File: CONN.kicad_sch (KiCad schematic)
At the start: 11 parts, among them J1 Conn_01x15, J2 Conn_01x15, J4 Conn_ARM_SWD_TagConnect_TC203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, J5 USB_C_Plug_USB2.0, U6 USBLC6-2P6

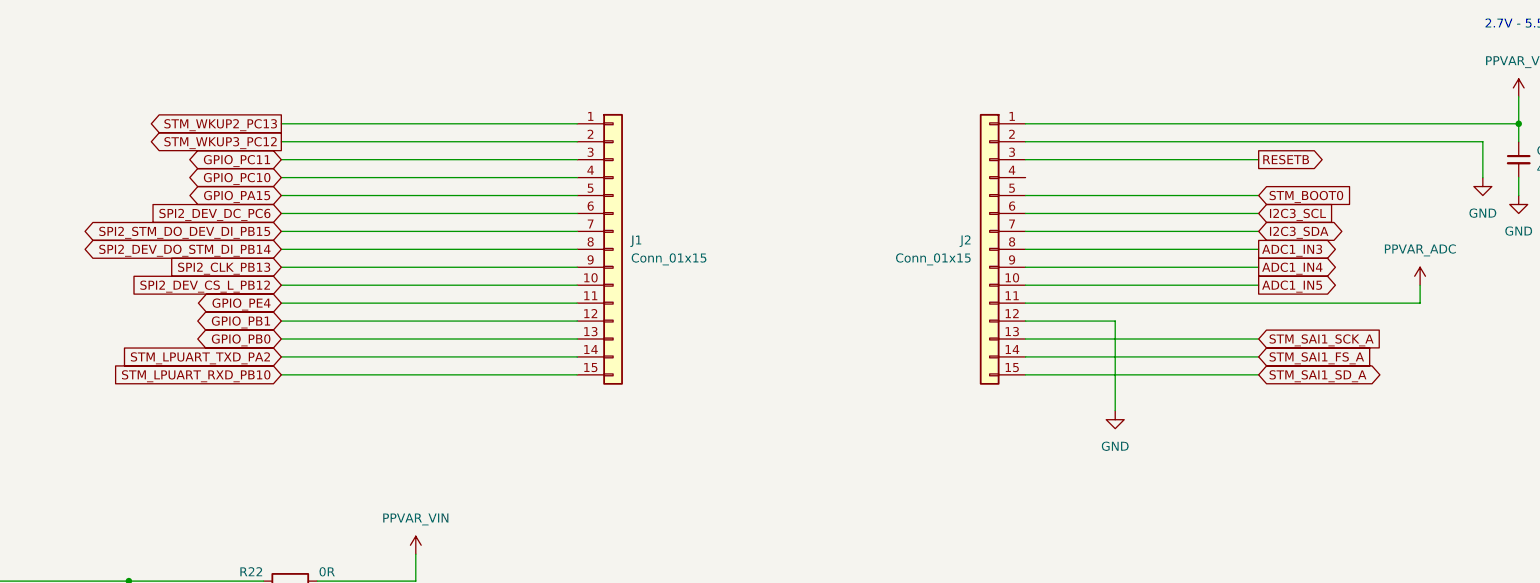
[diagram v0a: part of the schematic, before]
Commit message: Adding outputs, updated some component values.
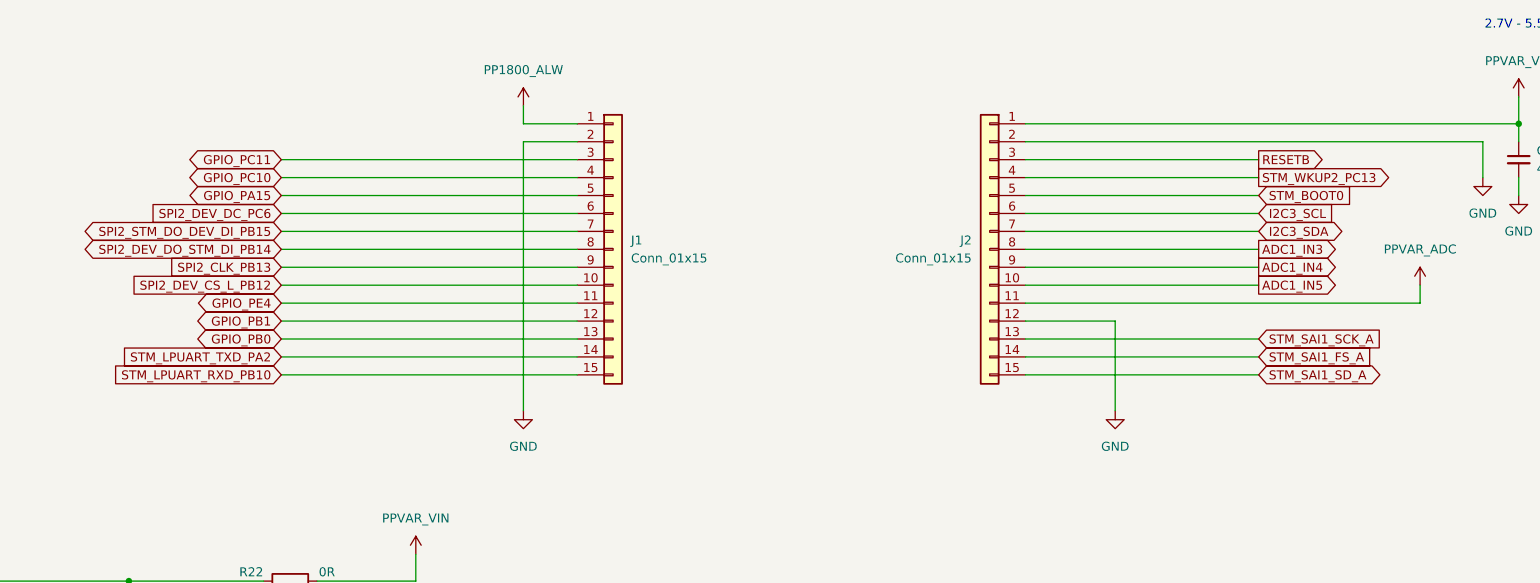
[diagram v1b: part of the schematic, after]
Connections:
- net STM_WKUP3_PC12 is gone; now on net GND: J1.2 (Pin_2)
- net STM_WKUP2_PC13: now also J2.4 (Pin_4); no longer J1.1 (Pin_1)
- new net PP1800_ALW: J1.1 (Pin_1)
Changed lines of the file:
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@@
 	(wire
 		(pts
-			(xy 185.42 48.26) (xy 143.51 48.26)
+			(xy 85.09 115.57) (xy 85.09 113.03)
 		)
 		(stroke
@@
 	(wire
 		(pts
-			(xy 85.09 115.57) (xy 85.09 113.03)
+			(xy 77.47 127) (xy 77.47 143.51)
 		)
 		(stroke
@@
 	(wire
 		(pts
-			(xy 77.47 127) (xy 77.47 143.51)
+			(xy 44.45 44.45) (xy 44.45 59.69)
 		)
 		(stroke
@@
 	(wire
 		(pts
-			(xy 44.45 44.45) (xy 44.45 59.69)
+			(xy 67.31 129.54) (xy 67.31 143.51)
 		)
 		(stroke
@@
 	(wire
 		(pts
-			(xy 67.31 129.54) (xy 67.31 143.51)
+			(xy 248.92 55.88) (xy 281.94 55.88)
 		)
 		(stroke
@@
 	(wire
 		(pts
+			(xy 177.8 48.26) (xy 185.42 48.26)
+		)
+		(stroke
+			(width 0)
+			(type default)
+		)
+	)
+	(wire
+		(pts
 			(xy 304.8 71.12) (xy 304.8 73.66)
 		)
@@
 	(wire
 		(pts
+			(xy 185.42 50.8) (xy 177.8 50.8)
+		)
+		(stroke
+			(width 0)
+			(type default)
+		)
+	)
+	(wire
+		(pts
 			(xy 101.6 138.43) (xy 116.84 138.43)
 		)
@@
 	(wire
 		(pts
+			(xy 177.8 45.72) (xy 177.8 48.26)
+		)
+		(stroke
+			(width 0)
+			(type default)
+		)
+	)
+	(wire
+		(pts
 			(xy 44.45 80.01) (xy 44.45 83.82)
 		)
@@
 	(wire
 		(pts
-			(xy 185.42 50.8) (xy 143.51 50.8)
+			(xy 177.8 50.8) (xy 177.8 88.9)
 		)
 		(stroke
@@
 		)
 	)
-	(global_label "STM_WKUP2_PC13"
-		(shape output)
-		(at 143.51 48.26 180)
-		(fields_autoplaced yes)
-		(effects
-			(font
-				(size 1.27 1.27)
-			)
-			(justify right)
-		)
-		(property "Intersheetrefs" "${INTERSHEET_REFS}"
-			(at 123.4707 48.26 0)
-			(effects
-				(font
-					(size 1.27 1.27)
-				)
-				(justify right)
-				(hide yes)
-			)
-		)
-	)
 	(global_label "RESETB"
 		(shape output)
@@
 		)
 	)
-	(global_label "STM_WKUP3_PC12"
-		(shape output)
-		(at 143.51 50.8 180)
-		(fields_autoplaced yes)
-		(effects
-			(font
-				(size 1.27 1.27)
-			)
-			(justify right)
-		)
-		(property "Intersheetrefs" "${INTERSHEET_REFS}"
-			(at 123.4707 50.8 0)
-			(effects
-				(font
-					(size 1.27 1.27)
-				)
-				(justify right)
-				(hide yes)
-			)
-		)
-	)
 	(global_label "SPI2_STM_DO_DEV_DI_PB15"
 		(shape bidirectional)
@@
 		)
 	)
+	(global_label "STM_WKUP2_PC13"
+		(shape output)
+		(at 281.94 55.88 0)
+		(fields_autoplaced yes)
+		(effects
+			(font
+				(size 1.27 1.27)
+			)
+			(justify left)
+		)
+		(property "Intersheetrefs" "${INTERSHEET_REFS}"
+			(at 301.9793 55.88 0)
+			(effects
+				(font
+					(size 1.27 1.27)
+				)
+				(justify left)
+				(hide yes)
+			)
+		)
+	)
 	(global_label "ADC1_IN5"
 		(shape output)
@@
 	)
 	(symbol
+		(lib_id "power:VCC")
+		(at 177.8 45.72 0)
+		(mirror y)
+		(unit 1)
+		(exclude_from_sim no)
+		(in_bom yes)
+		(on_board yes)
+		(dnp no)
+		(fields_autoplaced yes)
+		(property "Reference" "#PWR086"
+			(at 177.8 49.53 0)
+			(effects
+				(font
+					(size 1.27 1.27)
+				)
+				(hide yes)
+			)
+		)
+		(property "Value" "PP1800_ALW"
+			(at 177.8 40.64 0)
+			(effects
+				(font
+					(size 1.27 1.27)
+				)
+			)
+		)
+		(property "Footprint" ""
+			(at 177.8 45.72 0)
+			(effects
+				(font
+					(size 1.27 1.27)
+				)
+				(hide yes)
+			)
+		)
+		(property "Datasheet" ""
+			(at 177.8 45.72 0)
+			(effects
+				(font
+					(size 1.27 1.27)
+				)
+				(hide yes)
+			)
+		)
+		(property "Description" "Power symbol creates a global label with name \"VCC\""
+			(at 177.8 45.72 0)
+			(effects
+				(font
+					(size 1.27 1.27)
+				)
+				(hide yes)
+			)
+		)
+		(pin "1"
+		)
+		(instances
+			(project "Bluetooth_OSHW"
+				(path "/45b78866-6047-4631-b3ef-230df13ace1e/d84593e0-78e2-42aa-87f9-65c79fa5b8e5"
+					(reference "#PWR086")
+					(unit 1)
+				)
+			)
+		)
+	)
+	(symbol
 		(lib_id "power:VBUS")
 		(at 71.12 109.22 0)
@@
 					(unit 1)
 				)
+			)
+		)
+	)
+	(symbol
+		(lib_id "power:GND")
+		(at 177.8 88.9 0)
+		(unit 1)
+		(exclude_from_sim no)
+		(in_bom yes)
+		(on_board yes)
+		(dnp no)
+		(fields_autoplaced yes)
+		(property "Reference" "#PWR077"
+			(at 177.8 95.25 0)
+			(effects
+				(font
+					(size 1.27 1.27)
+				)
+				(hide yes)
+			)
+		)
+		(property "Value" "GND"
+			(at 177.8 93.98 0)
+			(effects
+				(font
+					(size 1.27 1.27)
+				)
+			)
+		)
+		(property "Footprint" ""
+			(at 177.8 88.9 0)
+			(effects
+				(font
+					(size 1.27 1.27)
+				)
+				(hide yes)
+			)
+		)
+		(property "Datasheet" ""
+			(at 177.8 88.9 0)
+			(effects
+				(font
+					(size 1.27 1.27)
+				)
+				(hide yes)
+			)
+		)
+		(property "Description" "Power symbol creates a global label with name \"GND\" , ground"
+			(at 177.8 88.9 0)
+			(effects
+				(font
+					(size 1.27 1.27)
+				)
+				(hide yes)
+			)
+		)
+		(pin "1"
+		)
+		(instances
+			(project "Bluetooth_OSHW"
+				(path "/45b78866-6047-4631-b3ef-230df13ace1e/d84593e0-78e2-42aa-87f9-65c79fa5b8e5"
+					(reference "#PWR077")
+					(unit 1)
+				)

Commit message: removed backup zips. adding updated output files
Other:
- title: nRF Battery Dev Kit -> stm32_bluet_pill
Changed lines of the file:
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@@
 	(paper "A3")
 	(title_block
-		(title "nRF Battery Dev Kit")
-		(date "2024-02-26")
+		(title "stm32_bluet_pill")
+		(date "2024-04-03")
 		(rev "Proto")
 		(company "Clover Designs")

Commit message: updating design files
updating schematics, gerbers, design files, etc.
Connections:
- net SWD_O: now reaches J4.6 (SWO)
- no-connect marks 3 -> 2

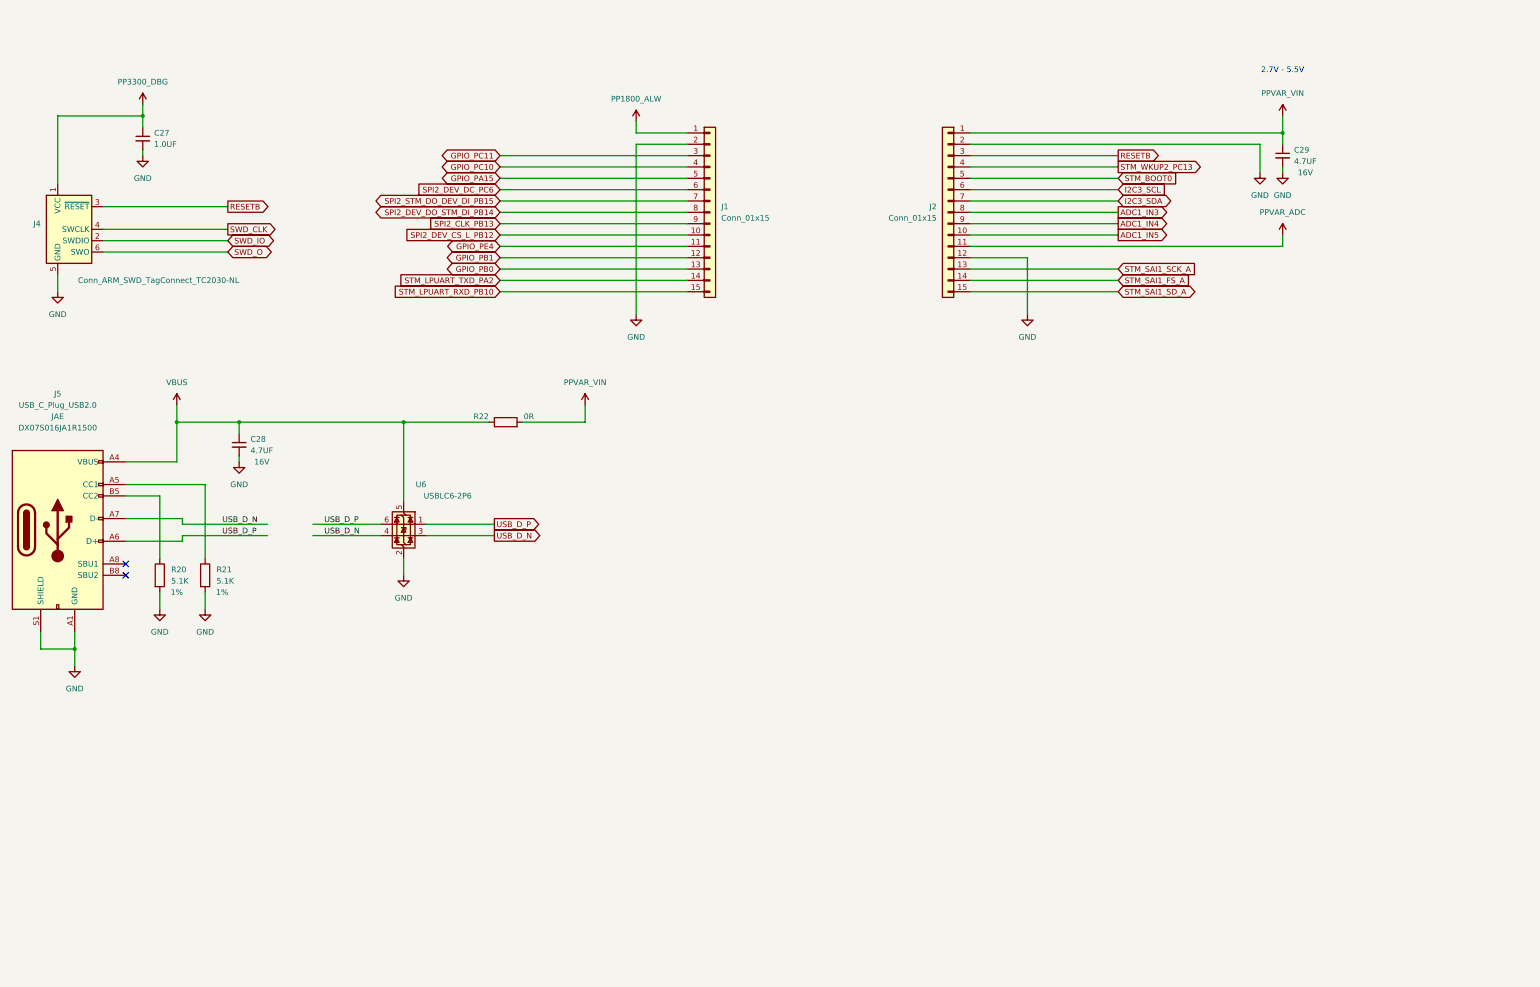
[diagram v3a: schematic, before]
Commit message: Updated project
- Changed board stackup, trace-widths
- Changed VIA size
- Fixed fab drawings
- added CHG FLT LED
- Removed unnecessary files
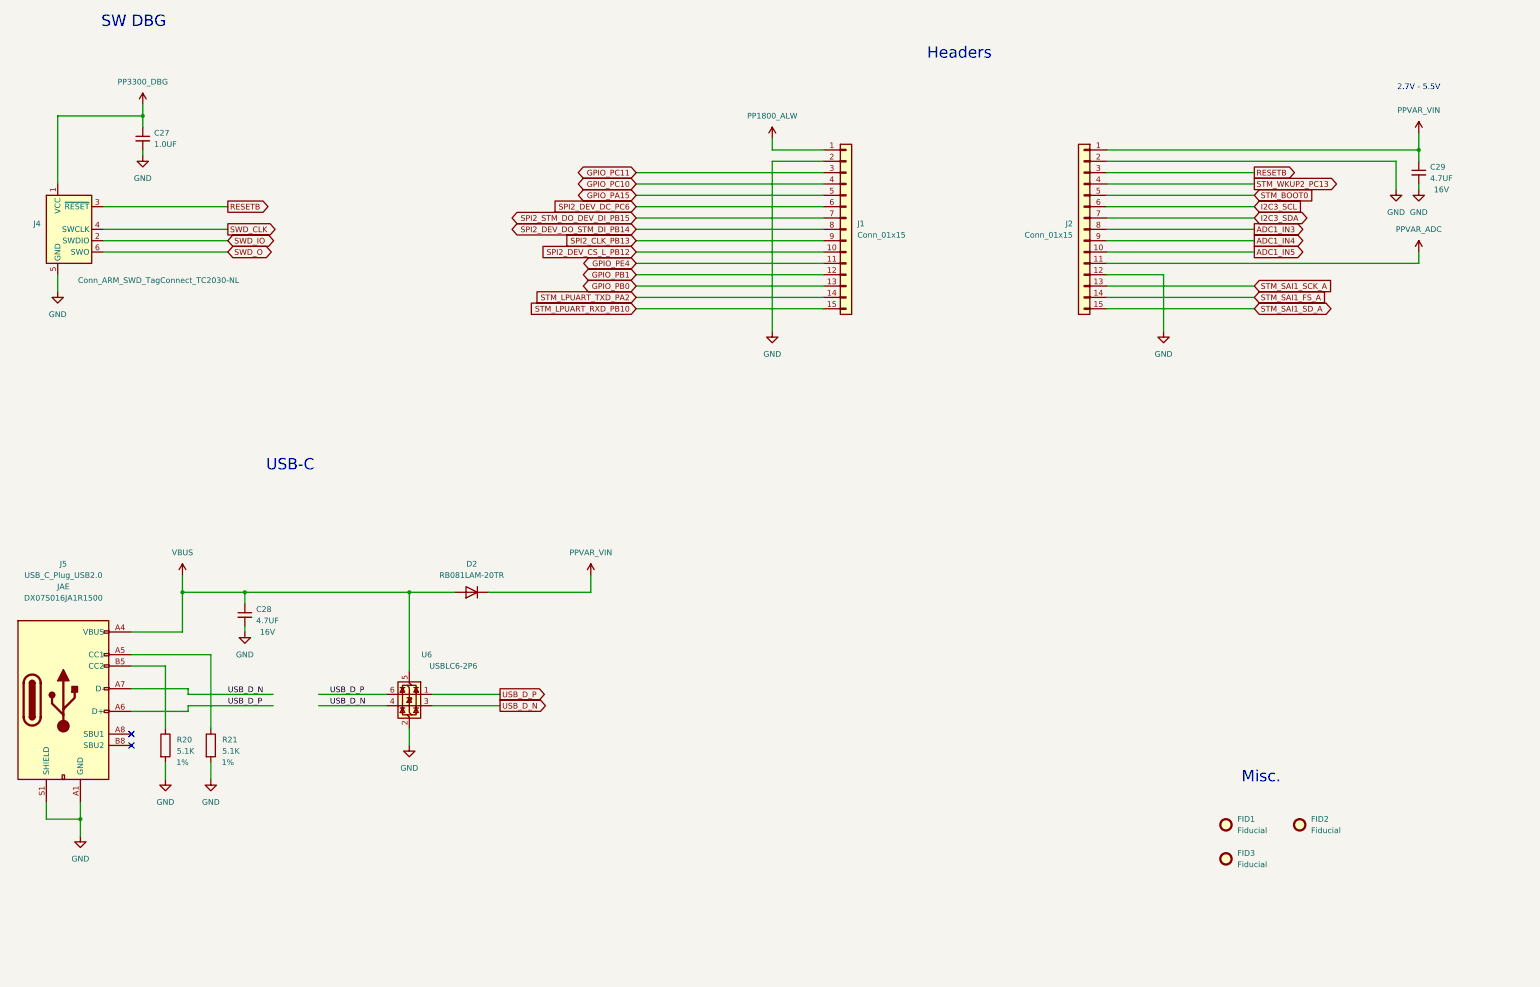
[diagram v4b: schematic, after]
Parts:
- removed R22: 0R, Resistor_SMD:R_0402_1005Metric, symbol Device:R
- added D2: RB081LAM-20TR, Diode_SMD:D_SOD-128, symbol Device:D
- added FID1, FID2, FID3: Fiducial, Fiducial:Fiducial_0.5mm_Mask1mm, symbol Mechanical:Fiducial
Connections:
- net PPVAR_VIN: now also D2.1 (K)
- net VBUS: now also D2.2 (A)
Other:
- note added: "Headers"
- note added: "Misc."
- note added: "SW DBG"
- note added: "USB-C"
- company: Clover Designs -> Brendan Bleker
- moved on the sheet: C28, C29, J1, J2, J5, R20, R21, U6

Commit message: Various BOM and Bug Fixes * Changed Stackup to common JLCPCB stackup * Modified trace widths as per new stackup * Reduced drill hole size * Rotated uFL connector as per datasheet pinout * Added pop options for ADC voltage * removed some GPIO and added GND to headers * BOM changes for battery charger, USB connector etc. to support component specifications and USB standards. * Improved MCU bypass and power delivery routing * Various other small bug fixes
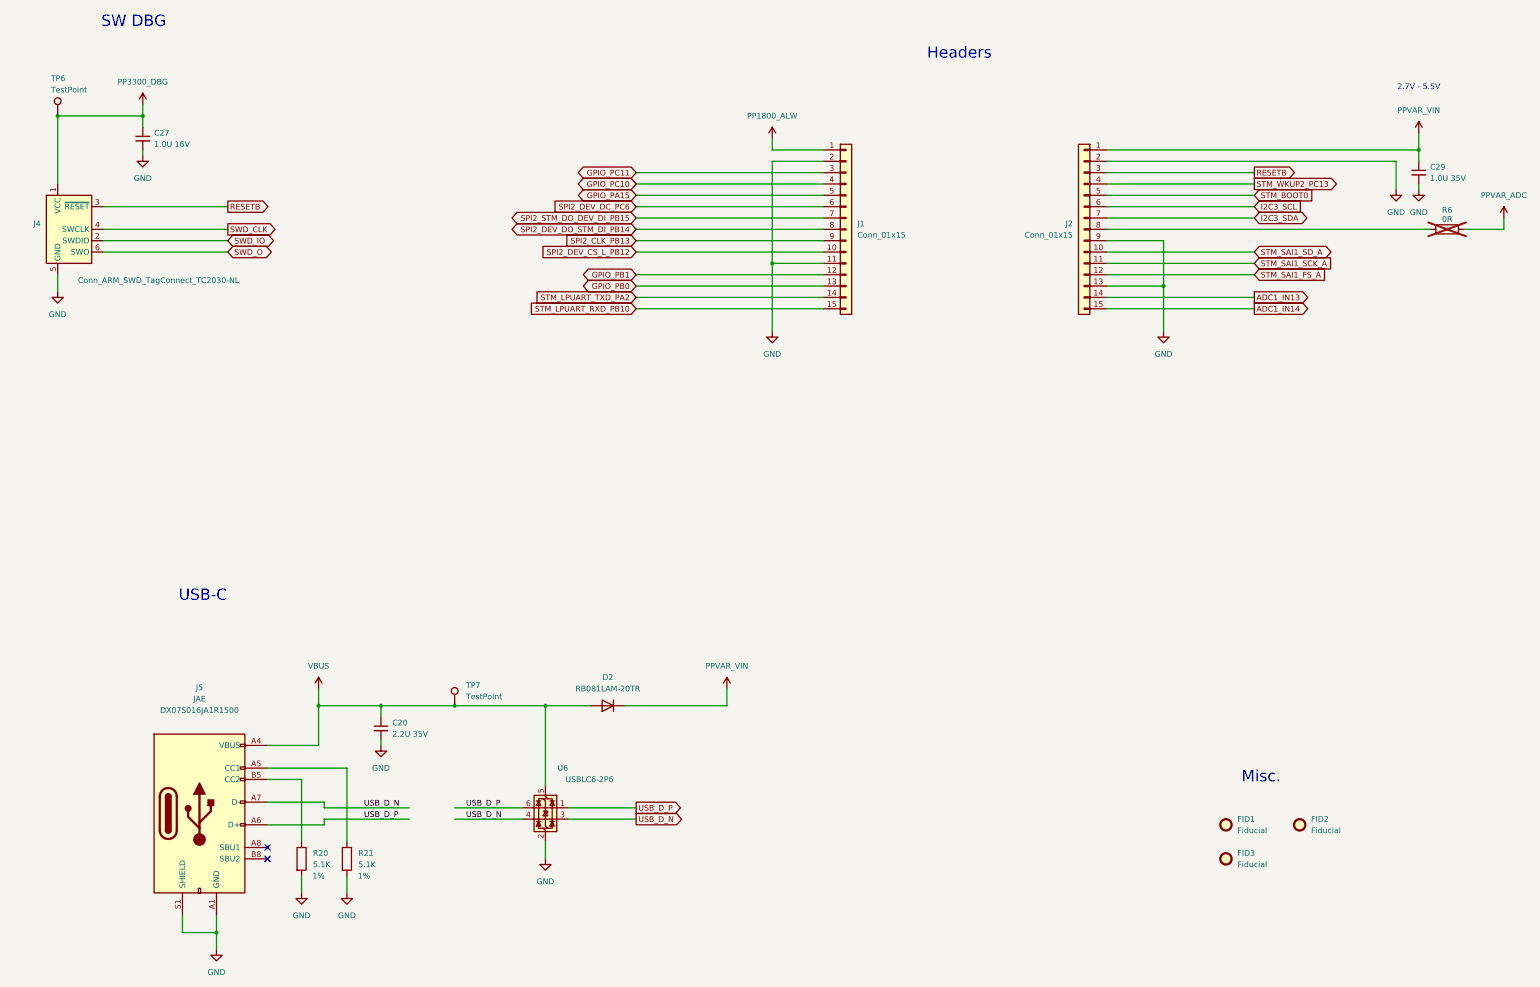
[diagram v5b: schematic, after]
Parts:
- removed C28: 4.7UF, Capacitor_SMD:C_0603_1608Metric, symbol Device:C_Small
- added C20: 2.2U 35V, Capacitor_SMD:C_0603_1608Metric, symbol Device:C_Small
- added R6: 0R, Resistor_SMD:R_0402_1005Metric, symbol Device:R
- added TP6, TP7: TestPoint, TestPoint:TestPoint_Pad_D1.0mm, symbol Connector:TestPoint
- C27: value 1.0UF -> 1.0U 16V
- C29: value 4.7UF -> 1.0U 35V; TOL 16V -> (none)
- J1, J2: now left out of the parts list
- J5: value USB_C_Plug_USB2.0 -> DX07S016JA1R1500
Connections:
- net ADC1_IN4 is gone; now on net GND: J2.9 (Pin_9)
- net ADC1_IN5 is gone; now on net STM_SAI1_SD_A: J2.10 (Pin_10)
- net GPIO_PE4 is gone; now on net GND: J1.11 (Pin_11)
- net GND: now also J2.13 (Pin_13), C20.2; no longer J2.12 (Pin_12)
- net PP3300_DBG: now also TP6.1
- net PPVAR_ADC: now also R6.1; no longer J2.11 (Pin_11)
- net STM_SAI1_FS_A: now also J2.12 (Pin_12); no longer J2.14 (Pin_14)
- net STM_SAI1_SCK_A: now also J2.11 (Pin_11); no longer J2.13 (Pin_13)
- net STM_SAI1_SD_A: no longer J2.15 (Pin_15)
- net VBUS: now also C20.1, TP7.1
- net ADC1_IN3: no longer names the net of J2.8 (Pin_8)
- net ADC1_IN3: now also R6.2
- new net ADC1_IN13: J2.14 (Pin_14)
- new net ADC1_IN14: J2.15 (Pin_15)
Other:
- moved on the sheet: D2, J5, R20, R21, U6
